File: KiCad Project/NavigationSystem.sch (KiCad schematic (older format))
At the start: 89 parts, among them J1 Screw_Terminal_01x02, J10 Conn_01x03, J11 Conn_01x03, J15 Conn_01x04, J16 Conn_01x03, J17 Conn_01x03, J18 Conn_01x03, J2 SWD, J3 Conn_01x04, J4 5-1814832-1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

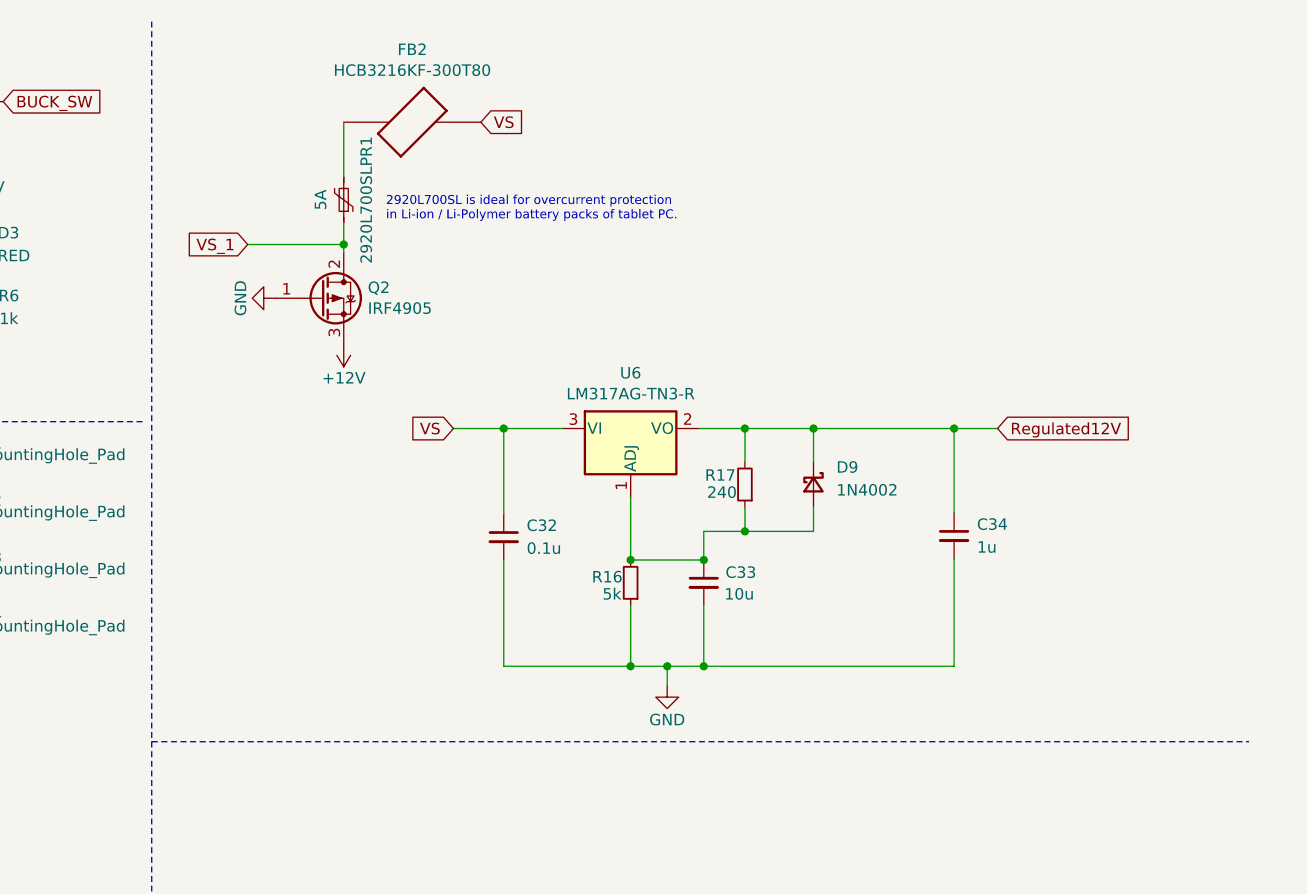
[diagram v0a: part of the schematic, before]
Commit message: power modules updated
reverse polarity protection
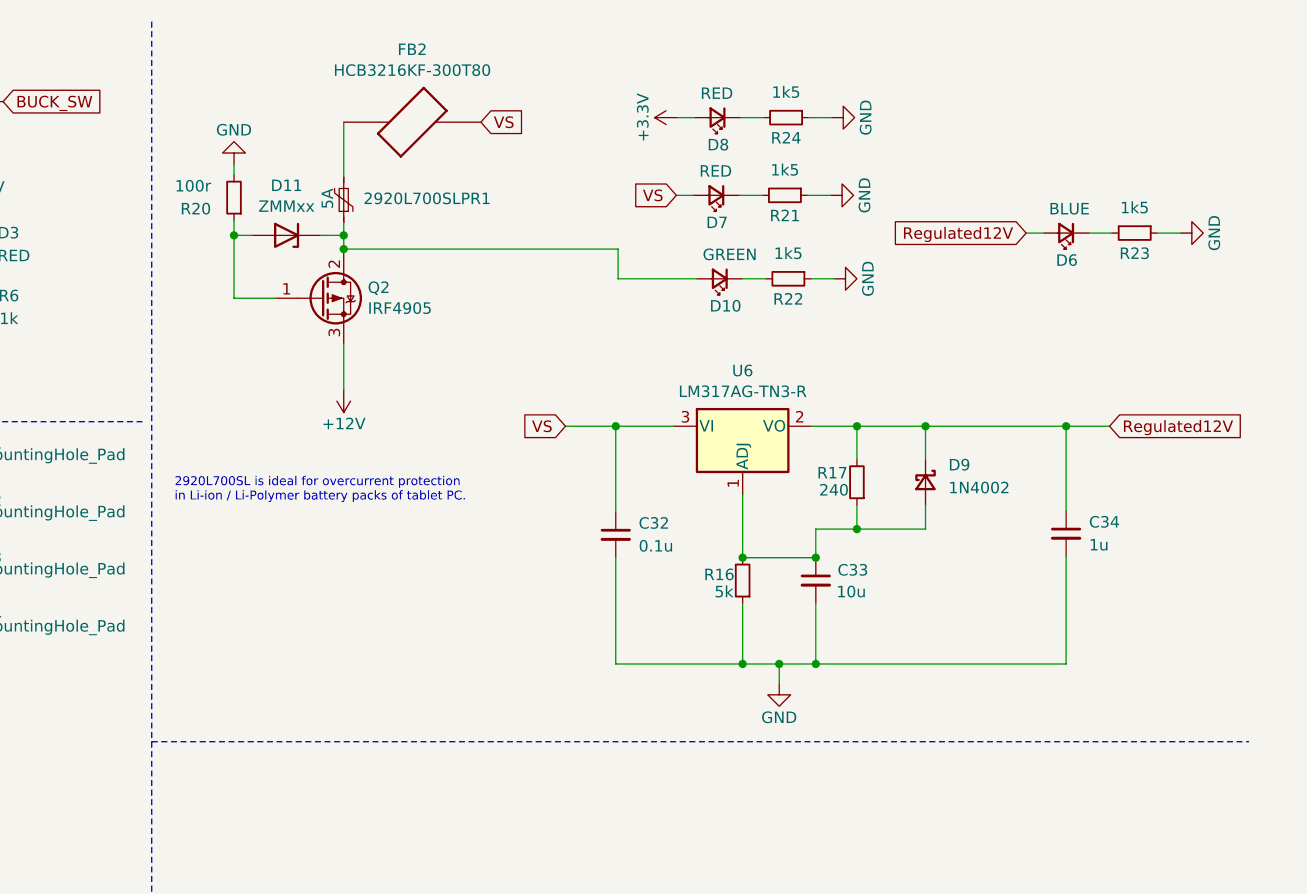
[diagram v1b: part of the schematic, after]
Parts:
- added D10: GREEN, LED_SMD:LED_0603_1608Metric, symbol Device:LED_Small
- added D11: ZMMxx, Diode_SMD:D_MiniMELF, symbol Diode:ZMMxx
- added D6: BLUE, LED_SMD:LED_0603_1608Metric, symbol Device:LED_Small
- added D7, D8: RED, LED_SMD:LED_0603_1608Metric, symbol Device:LED_Small
- added R20: 100r, Resistor_SMD:R_0603_1608Metric, symbol Device:R_Small
- added R21, R22, R23, R24: 1k5, Resistor_SMD:R_0603_1608Metric, symbol Device:R_Small
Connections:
- net +3V3: now also D8.2 (A)
- net GND: now also R20.2, R21.1, R22.1, R23.1, R24.1; no longer Q2.1 (G)
- net Regulated12V: now also D6.2 (A)
- net VS: now also D7.2 (A)
- net VS_1: no longer names the net of 2920L700SLPR1.1, Q2.2 (D)
- net VS_1: now also D10.2 (A), D11.1 (K)
- new net: D11.2 (A), Q2.1 (G), R20.1
- new net: D7.1 (K), R21.2
- new net: D10.1 (K), R22.2
- new net: D6.1 (K), R23.2
- new net: D8.1 (K), R24.2
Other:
- moved on the sheet: C32, C33, C34, D9, R16, R17, U6
